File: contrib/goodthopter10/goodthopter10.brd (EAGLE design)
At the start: 54.3 x 21.6 mm, 15 parts, among them IC1 F22X4---DA38, IC2 FT232RL-BASICSSOP, Q1 20MHz

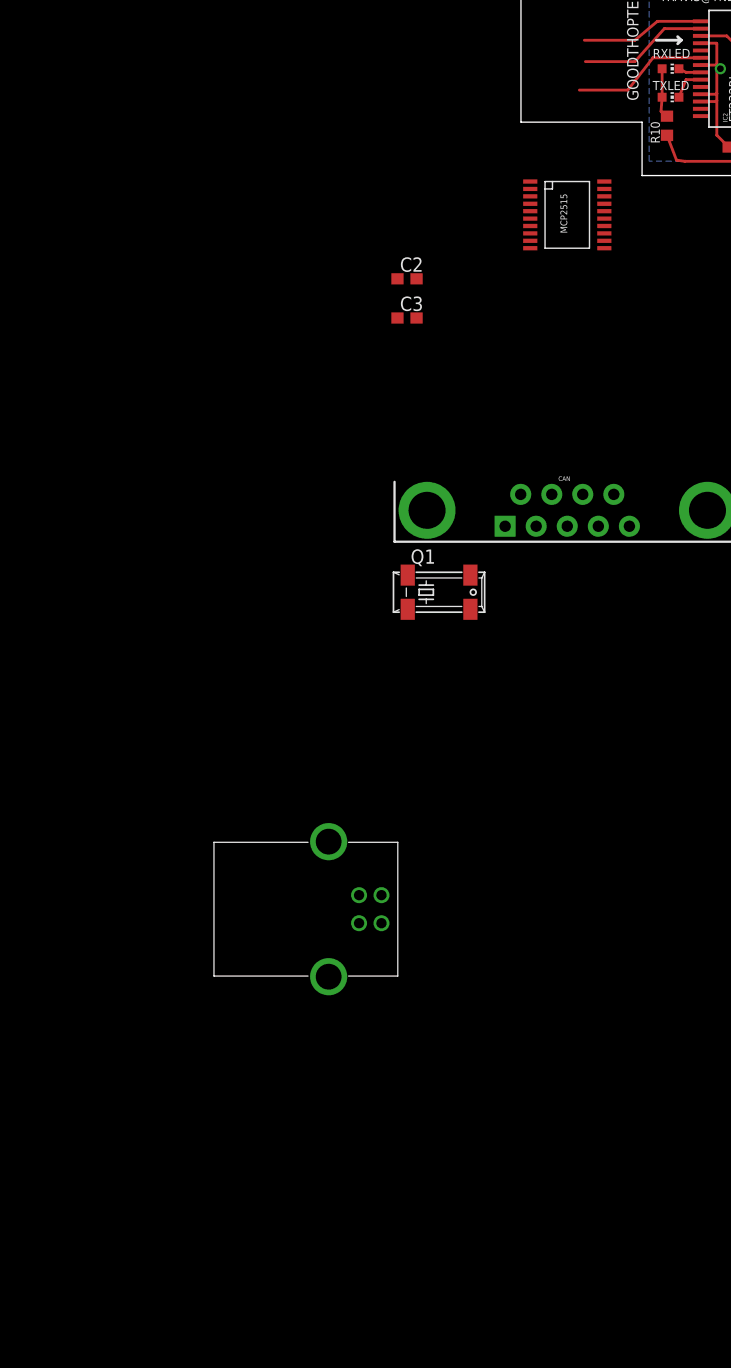
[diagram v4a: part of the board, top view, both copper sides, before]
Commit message: Updated schematic /goodthopter10, added CAN_IO, MCP2551 and Low/High Voltage options.
git-svn-id: https://svn.code.sf.net/p/goodfet/code@1199 12e2690d-a6be-4b82-a7b7-67c4a43b65c8
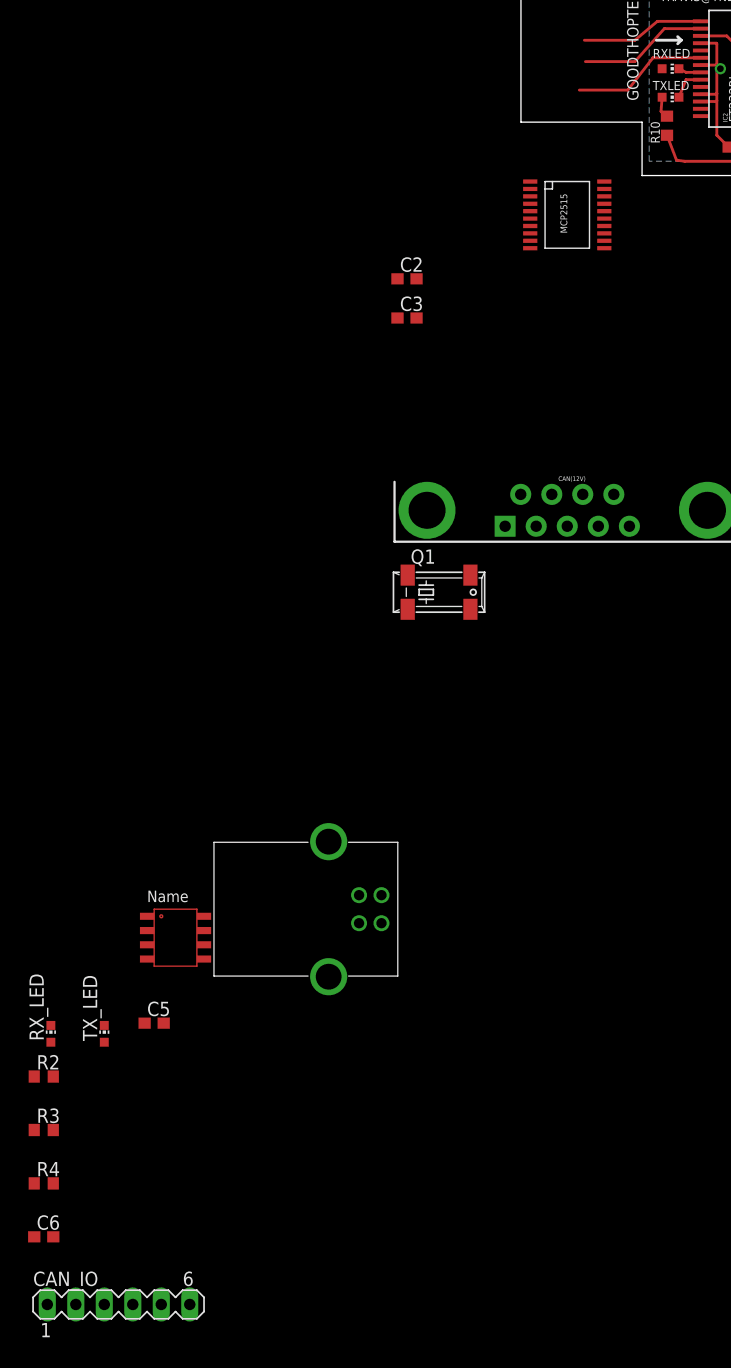
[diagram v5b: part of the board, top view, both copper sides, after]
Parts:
- added C5, C6: 0.1uF, rcl:C0603
- added CAN_IO: (no value), con-lstb:MA06-1
- added R2, R3: 470, rcl:R0603
- added R4: 10k, rcl:R0603
- added RX_LED, TX_LED: (no value), led:CHIP-LED0603
- added U$2: MCP2551, MCP2551:SOIC-8
- renumbered CAN to CAN(12V)
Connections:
- new net !TX0RTS: CAN_IO.4, U$1.4
- new net !TX1RTS: CAN_IO.5, U$1.5
- new net !TX2RTS: CAN_IO.6, U$1.7
- new net CANH: CAN(12V).7, U$2.CANH
- new net CANL: CAN(12V).2, U$2.CANL
- new net CLKOUT: CAN_IO.3, U$1.3
- new net N$1: R2.2, RX_LED.A
- new net N$11: C6.2, R4.1
- new net N$2: R3.2, TX_LED.A
- new net N$5: R4.2, U$1.19
- net !CS: no longer U$1.18
- net GND: now also C5.1, C6.1, U$2.RS, U$2.VSS
- net RXCAN: now also CAN_IO.2, RX_LED.C, U$2.RXD; no longer CAN(12V).2
- net TXCAN: now also CAN_IO.1, TX_LED.C, U$2.TXD; no longer CAN(12V).7
- net VCC: now also R2.1, R3.1; no longer U$1.19
- net VCC5V: now also C5.2, U$2.VDD
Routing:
- net N$8: track 4.49 -> 1.95 mm
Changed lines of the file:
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@@
 <element name="C2" library="rcl" package="C0603" value="15pF" x="-10.16" y="-8.89"/>
 <element name="C3" library="rcl" package="C0603" value="15pF" x="-10.16" y="-12.3825"/>
-<element name="CAN" library="SparkFun-Connectors" package="DB9_MALE" value="" x="4.1275" y="-29.5275"/>
+<element name="CAN(12V)" library="SparkFun-Connectors" package="DB9_MALE" value="" x="4.1275" y="-29.5275"/>
 <element name="Q1" library="crystal" package="MM20SS" value="20MHz" x="-7.3025" y="-36.83">
 <attribute name="OC_NEWARK" value="unknown" x="-7.3025" y="-36.83" size="1.778" layer="27" display="off"/>
@@
 <attribute name="OC_FARNELL" value="unknown" x="-17.145" y="-65.0875" size="1.778" layer="27" display="off"/>
 </element>
+<element name="U$2" library="MCP2551" package="SOIC-8" value="MCP2551" x="-30.7975" y="-67.6275"/>
+<element name="C5" library="rcl" package="C0603" value="0.1uF" x="-32.7025" y="-75.2475"/>
+<element name="TX_LED" library="led" package="CHIP-LED0603" value="" x="-37.1475" y="-76.2"/>
+<element name="RX_LED" library="led" package="CHIP-LED0603" value="" x="-41.91" y="-76.2"/>
+<element name="R2" library="rcl" package="R0603" value="470" x="-42.545" y="-80.01"/>
+<element name="R3" library="rcl" package="R0603" value="470" x="-42.545" y="-84.7725"/>
+<element name="R4" library="rcl" package="R0603" value="10k" x="-42.545" y="-89.535"/>
+<element name="C6" library="rcl" package="C0603" value="0.1uF" x="-42.545" y="-94.2975"/>
+<element name="CAN_IO" library="con-lstb" package="MA06-1" value="" x="-35.8775" y="-100.33">
+<attribute name="OC_NEWARK" value="unknown" x="-35.8775" y="-100.33" size="1.778" layer="27" display="off"/>
+<attribute name="MPN" value="" x="-35.8775" y="-100.33" size="1.778" layer="27" display="off"/>
+<attribute name="MF" value="" x="-35.8775" y="-100.33" size="1.778" layer="27" display="off"/>
+<attribute name="OC_FARNELL" value="unknown" x="-35.8775" y="-100.33" size="1.778" layer="27" display="off"/>
+</element>
 </elements>
 <signals>
@@
 <wire x1="49.2125" y1="9.8425" x2="49.8475" y2="10.4775" width="0.254" layer="1"/>
 <wire x1="49.8475" y1="10.4775" x2="49.8475" y2="12.3825" width="0.254" layer="1"/>
-<contactref element="U$1" pad="18"/>
-<wire x1="7.4295" y1="-1.5367" x2="38.0925" y2="9.54" width="0" layer="19" extent="1-1"/>
 </signal>
 <signal name="MOSI">
@@
 <via x="20.32" y="7.3025" extent="1-16" drill="0.6" shape="square"/>
 <via x="34.6075" y="3.81" extent="1-16" drill="0.6" shape="square"/>
+<contactref element="R2" pad="1"/>
+<contactref element="R3" pad="1"/>
 <contactref element="U$1" pad="20"/>
-<contactref element="U$1" pad="19"/>
-<wire x1="7.4295" y1="-0.2159" x2="13.8675" y2="1.69" width="0" layer="19" extent="1-1"/>
-<wire x1="7.4295" y1="-0.8763" x2="7.4295" y2="-0.2159" width="0" layer="19" extent="1-1"/>
+<wire x1="-43.395" y1="-80.01" x2="-43.395" y2="-84.7725" width="0" layer="19" extent="1-1"/>
+<wire x1="7.4295" y1="-0.2159" x2="-43.395" y2="-80.01" width="0" layer="19" extent="1-1"/>
+<wire x1="13.8675" y1="1.69" x2="7.4295" y2="-0.2159" width="0" layer="19" extent="1-1"/>
 </signal>
 <signal name="RXD">
@@
 <contactref element="C2" pad="1"/>
 <contactref element="C3" pad="1"/>
-<contactref element="CAN" pad="3"/>
+<contactref element="CAN(12V)" pad="3"/>
 <contactref element="U$1" pad="10"/>
 <contactref element="292304-2" pad="4"/>
+<contactref element="U$2" pad="RS"/>
+<contactref element="U$2" pad="VSS"/>
+<contactref element="C5" pad="1"/>
+<contactref element="C6" pad="1"/>
+<wire x1="-33.5525" y1="-75.2475" x2="-43.395" y2="-94.2975" width="0" layer="19" extent="1-1"/>
+<wire x1="-33.3375" y1="-66.9925" x2="-33.5525" y2="-75.2475" width="0" layer="19" extent="1-1"/>
+<wire x1="-28.2575" y1="-65.7225" x2="-33.3375" y2="-66.9925" width="0" layer="19" extent="1-1"/>
+<wire x1="-14.435" y1="-66.3375" x2="-28.2575" y2="-65.7225" width="0" layer="19" extent="1-1"/>
 <wire x1="4.1275" y1="-30.9475" x2="-14.435" y2="-66.3375" width="0" layer="19" extent="1-1"/>
 <wire x1="-11.01" y1="-12.3825" x2="4.1275" y2="-30.9475" width="0" layer="19" extent="1-1"/>
@@
 </signal>
 <signal name="N$8">
-<contactref element="RXLED" pad="A"/>
 <contactref element="TXLED" pad="A"/>
 <contactref element="R10" pad="1"/>
-<wire x1="12.585" y1="7.3025" x2="12.585" y2="9.8425" width="0.254" layer="1"/>
 <wire x1="12.585" y1="7.3025" x2="12.485" y2="6.0325" width="0.254" layer="1"/>
 <wire x1="12.485" y1="6.0325" x2="13.0175" y2="5.6125" width="0.254" layer="1"/>
+<contactref element="RXLED" pad="A"/>
+<wire x1="12.585" y1="7.3025" x2="12.585" y2="9.8425" width="0" layer="19" extent="1-1"/>
 </signal>
 <signal name="RTS">
@@
 <wire x1="5.205" y1="7.9375" x2="9.525" y2="7.9375" width="0.254" layer="1"/>
 <contactref element="292304-2" pad="1"/>
+<contactref element="U$2" pad="VDD"/>
+<contactref element="C5" pad="2"/>
+<wire x1="-33.3375" y1="-68.2625" x2="-31.8525" y2="-75.2475" width="0" layer="19" extent="1-1"/>
+<wire x1="-12.435" y1="-66.3375" x2="-33.3375" y2="-68.2625" width="0" layer="19" extent="1-1"/>
 <wire x1="5.205" y1="7.9375" x2="-12.435" y2="-66.3375" width="0" layer="19" extent="1-1"/>
 </signal>
@@
 <signal name="TXCAN">
 <contactref element="U$1" pad="1"/>
-<contactref element="CAN" pad="7"/>
-<wire x1="0.8255" y1="-0.2159" x2="5.5075" y2="-28.1075" width="0" layer="19" extent="1-1"/>
+<contactref element="U$2" pad="TXD"/>
+<contactref element="TX_LED" pad="C"/>
+<contactref element="CAN_IO" pad="1"/>
+<wire x1="-37.1475" y1="-75.45" x2="-42.2275" y2="-100.33" width="0" layer="19" extent="1-1"/>
+<wire x1="-33.3375" y1="-65.7225" x2="-37.1475" y2="-75.45" width="0" layer="19" extent="1-1"/>
+<wire x1="0.8255" y1="-0.2159" x2="-33.3375" y2="-65.7225" width="0" layer="19" extent="1-1"/>
 </signal>
 <signal name="RXCAN">
 <contactref element="U$1" pad="2"/>
-<contactref element="CAN" pad="2"/>
-<wire x1="0.8255" y1="-0.8763" x2="6.8975" y2="-30.9475" width="0" layer="19" extent="1-1"/>
+<contactref element="U$2" pad="RXD"/>
+<contactref element="RX_LED" pad="C"/>
+<contactref element="CAN_IO" pad="2"/>
+<wire x1="-41.91" y1="-75.45" x2="-39.6875" y2="-100.33" width="0" layer="19" extent="1-1"/>
+<wire x1="-33.3375" y1="-69.5325" x2="-41.91" y2="-75.45" width="0" layer="19" extent="1-1"/>
+<wire x1="0.8255" y1="-0.8763" x2="-33.3375" y2="-69.5325" width="0" layer="19" extent="1-1"/>
 </signal>
 <signal name="!INT">
@@
 </signal>
 <signal name="GND_OPT">
-<contactref element="CAN" pad="6"/>
+<contactref element="CAN(12V)" pad="6"/>
 </signal>
 <signal name="RSRVD2">
-<contactref element="CAN" pad="8"/>
+<contactref element="CAN(12V)" pad="8"/>
 </signal>
 <signal name="CAN_V+_OPT">
-<contactref element="CAN" pad="9"/>
+<contactref element="CAN(12V)" pad="9"/>
 </signal>
 <signal name="CAN_SHLD">
-<contactref element="CAN" pad="5"/>
+<contactref element="CAN(12V)" pad="5"/>
 </signal>
 <signal name="RSRVD1">
-<contactref element="CAN" pad="4"/>
+<contactref element="CAN(12V)" pad="4"/>
 </signal>
 <signal name="RSRVD0">
-<contactref element="CAN" pad="1"/>
+<contactref element="CAN(12V)" pad="1"/>
+</signal>
+<signal name="CANL">
+<contactref element="U$2" pad="CANL"/>
+<contactref element="CAN(12V)" pad="2"/>
+<wire x1="6.8975" y1="-30.9475" x2="-28.2575" y2="-68.2625" width="0" layer="19" extent="1-1"/>
+</signal>
+<signal name="CANH">
+<contactref element="U$2" pad="CANH"/>
+<contactref element="CAN(12V)" pad="7"/>
+<wire x1="5.5075" y1="-28.1075" x2="-28.2575" y2="-66.9925" width="0" layer="19" extent="1-1"/>
+</signal>
+<signal name="N$1">
+<contactref element="RX_LED" pad="A"/>
+<contactref element="R2" pad="2"/>
+<wire x1="-41.91" y1="-76.95" x2="-41.695" y2="-80.01" width="0" layer="19" extent="1-1"/>
+</signal>
+<signal name="N$2">
+<contactref element="TX_LED" pad="A"/>
+<contactref element="R3" pad="2"/>
+<wire x1="-37.1475" y1="-76.95" x2="-41.695" y2="-84.7725" width="0" layer="19" extent="1-1"/>
+</signal>
+<signal name="N$5">
+<contactref element="U$1" pad="19"/>
+<contactref element="R4" pad="2"/>
+<wire x1="7.4295" y1="-0.8763" x2="-41.695" y2="-89.535" width="0" layer="19" extent="1-1"/>
+</signal>
+<signal name="N$11">
+<contactref element="R4" pad="1"/>
+<contactref element="C6" pad="2"/>
+<wire x1="-43.395" y1="-89.535" x2="-41.695" y2="-94.2975" width="0" layer="19" extent="1-1"/>
+</signal>
+<signal name="CLKOUT">
+<contactref element="CAN_IO" pad="3"/>
+<contactref element="U$1" pad="3"/>
+<wire x1="0.8255" y1="-1.5367" x2="-37.1475" y2="-100.33" width="0" layer="19" extent="1-1"/>
+</signal>
+<signal name="!TX0RTS">
+<contactref element="U$1" pad="4"/>
+<contactref element="CAN_IO" pad="4"/>
+<wire x1="0.8255" y1="-2.1971" x2="-34.6075" y2="-100.33" width="0" layer="19" extent="1-1"/>
+</signal>
+<signal name="!TX1RTS">
+<contactref element="U$1" pad="5"/>
+<contactref element="CAN_IO" pad="5"/>
+<wire x1="0.8255" y1="-2.8575" x2="-32.0675" y2="-100.33" width="0" layer="19" extent="1-1"/>
+</signal>
+<signal name="!TX2RTS">
+<contactref element="U$1" pad="7"/>
+<contactref element="CAN_IO" pad="6"/>
+<wire x1="0.8255" y1="-4.1783" x2="-29.5275" y2="-100.33" width="0" layer="19" extent="1-1"/>
 </signal>
 </signals>
